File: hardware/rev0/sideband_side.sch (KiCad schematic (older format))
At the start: 10 parts, among them IC1 ECP5-BGA256, U8 USB3343

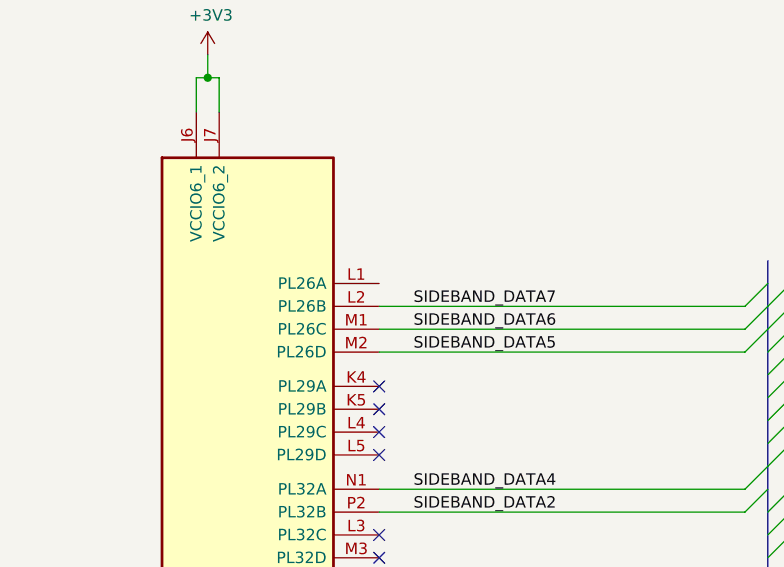
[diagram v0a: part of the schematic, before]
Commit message: Route/NC remaining target signals, ERC & schematic cleanup
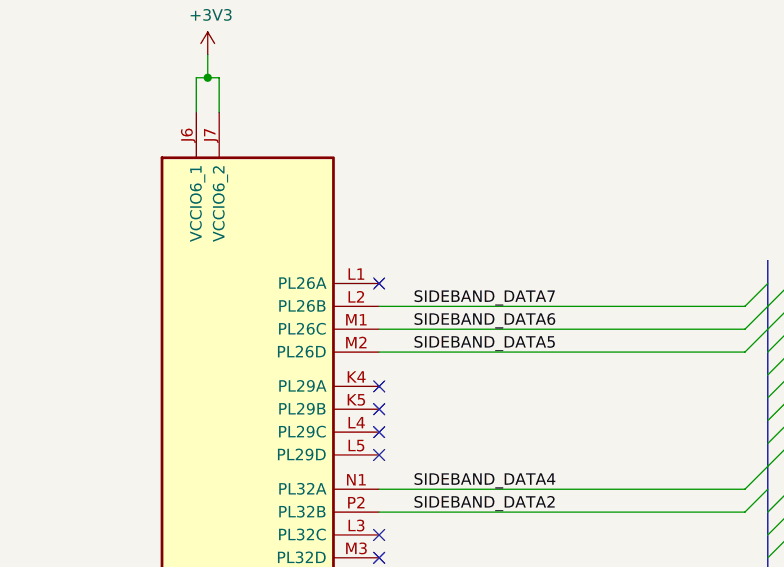
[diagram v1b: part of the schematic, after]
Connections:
- no-connect marks 19 -> 20
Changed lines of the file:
@@
 Wire Wire Line
 	6750 4050 7150 4050
+NoConn ~ 2500 2450
 Wire Bus Line
 	4200 2350 4200 5450

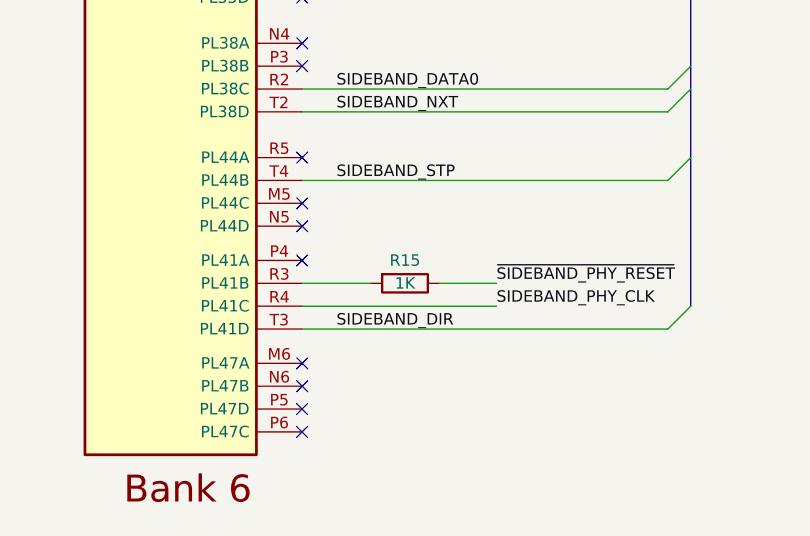
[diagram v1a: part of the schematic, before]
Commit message: Tidy up component values
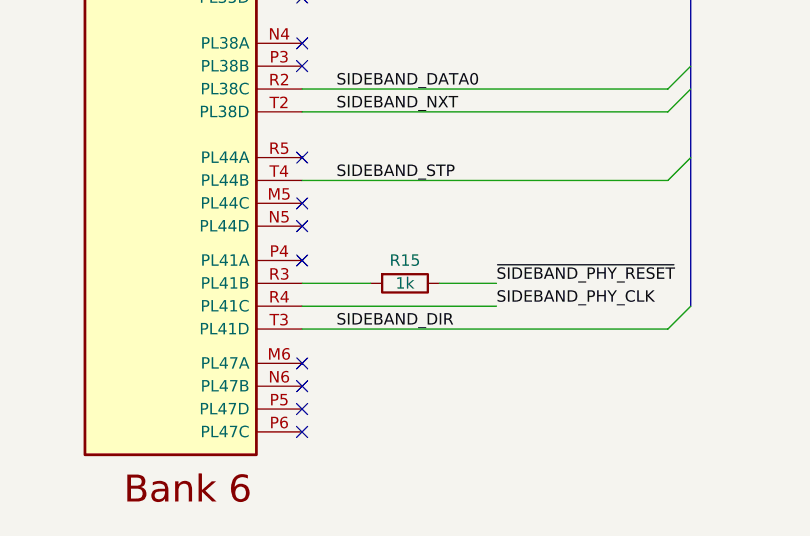
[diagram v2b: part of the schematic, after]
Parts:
- R15: value 1K -> 1k
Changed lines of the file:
@@
 P 2950 5350
 F 0 "R15" V 2850 5350 50  0000 C CNN
-F 1 "1K" V 2950 5350 50  0000 C CNN
+F 1 "1k" V 2950 5350 50  0000 C CNN
 F 2 "Resistor_SMD:R_0402_1005Metric" V 2880 5350 50  0001 C CNN
 F 3 "~" H 2950 5350 50  0001 C CNN

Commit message: Pick part numbers for BOM
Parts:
- C36, C37: Manufacturer_Part_Number (none) -> LMK107B7225KA-T
- C38, C39: Manufacturer_Part_Number (none) -> LMF105B7104KVHF
- R15: Manufacturer_Part_Number (none) -> CRCW04021K00FKEDC
- R16: Manufacturer_Part_Number (none) -> CRCW04028K06FKED
- R17: Manufacturer_Part_Number (none) -> CRCW040220K0FKEDC
- R22: Manufacturer_Part_Number (none) -> CRCW040215K0FKEDC
- U8: Manufacturer_Part_Number (none) -> USB3343-CP-TR
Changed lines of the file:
@@
 F 2 "Package_DFN_QFN:VQFN-24-1EP_4x4mm_P0.5mm_EP2.45x2.45mm" H 5450 2350 50  0001 C CNN
 F 3 "http://ww1.microchip.com/downloads/en/DeviceDoc/334x.pdf" H 5450 2350 50  0001 C CNN
+F 4 "USB3343-CP-TR" H 5450 2350 50  0001 C CNN "Manufacturer_Part_Number"
 	1    5450 2350
 	1    0    0    -1
@@
 F 2 "Capacitor_SMD:C_0603_1608Metric" H 7188 4050 50  0001 C CNN
 F 3 "~" H 7150 4200 50  0001 C CNN
+F 4 "LMK107B7225KA-T" H 7150 4200 50  0001 C CNN "Manufacturer_Part_Number"
 	1    7150 4200
 	1    0    0    -1
@@
 F 2 "Capacitor_SMD:C_0603_1608Metric" H 7638 4050 50  0001 C CNN
 F 3 "~" H 7600 4200 50  0001 C CNN
+F 4 "LMK107B7225KA-T" H 7600 4200 50  0001 C CNN "Manufacturer_Part_Number"
 	1    7600 4200
 	1    0    0    -1
@@
 F 2 "Resistor_SMD:R_0402_1005Metric" V 6980 3400 50  0001 C CNN
 F 3 "~" H 7050 3400 50  0001 C CNN
+F 4 "CRCW04028K06FKED" H 7050 3400 50  0001 C CNN "Manufacturer_Part_Number"
 	1    7050 3400
 	0    1    1    0
@@
 F 2 "Resistor_SMD:R_0402_1005Metric" V 7030 2850 50  0001 C CNN
 F 3 "~" H 7100 2850 50  0001 C CNN
+F 4 "CRCW040220K0FKEDC" H 7100 2850 50  0001 C CNN "Manufacturer_Part_Number"
 	1    7100 2850
 	0    1    1    0
@@
 F 2 "Capacitor_SMD:C_0402_1005Metric" H 8638 1400 50  0001 C CNN
 F 3 "~" H 8600 1550 50  0001 C CNN
+F 4 "LMF105B7104KVHF" H 8600 1550 50  0001 C CNN "Manufacturer_Part_Number"
 	1    8600 1550
 	1    0    0    -1
@@
 F 2 "Capacitor_SMD:C_0402_1005Metric" H 9138 1400 50  0001 C CNN
 F 3 "~" H 9100 1550 50  0001 C CNN
+F 4 "LMF105B7104KVHF" H 9100 1550 50  0001 C CNN "Manufacturer_Part_Number"
 	1    9100 1550
 	1    0    0    -1
@@
 F 2 "Resistor_SMD:R_0402_1005Metric" V 2880 5350 50  0001 C CNN
 F 3 "~" H 2950 5350 50  0001 C CNN
+F 4 "CRCW04021K00FKEDC" H 2950 5350 50  0001 C CNN "Manufacturer_Part_Number"
 	1    2950 5350
 	0    1    1    0
@@
 F 2 "Resistor_SMD:R_0402_1005Metric" V 4830 4600 50  0001 C CNN
 F 3 "~" H 4900 4600 50  0001 C CNN
+F 4 "CRCW040215K0FKEDC" H 4900 4600 50  0001 C CNN "Manufacturer_Part_Number"
 	1    4900 4600
 	-1   0    0    1
